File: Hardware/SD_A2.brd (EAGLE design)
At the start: 100.2 x 77.7 mm, 31 parts, among them IC1 74LS245N, IC2 LM317, IC4 XC9572XL, IC5 28C64ASO

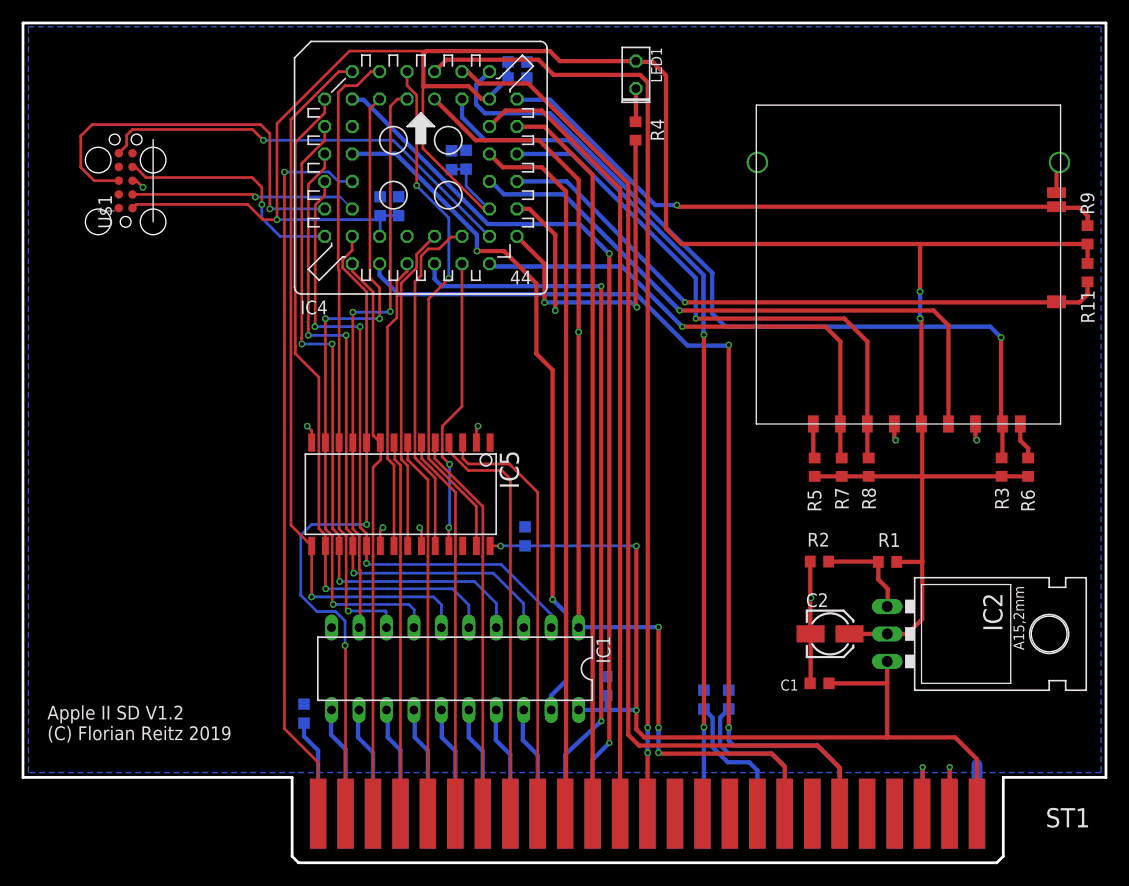
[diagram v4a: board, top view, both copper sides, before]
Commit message: Resistor network added
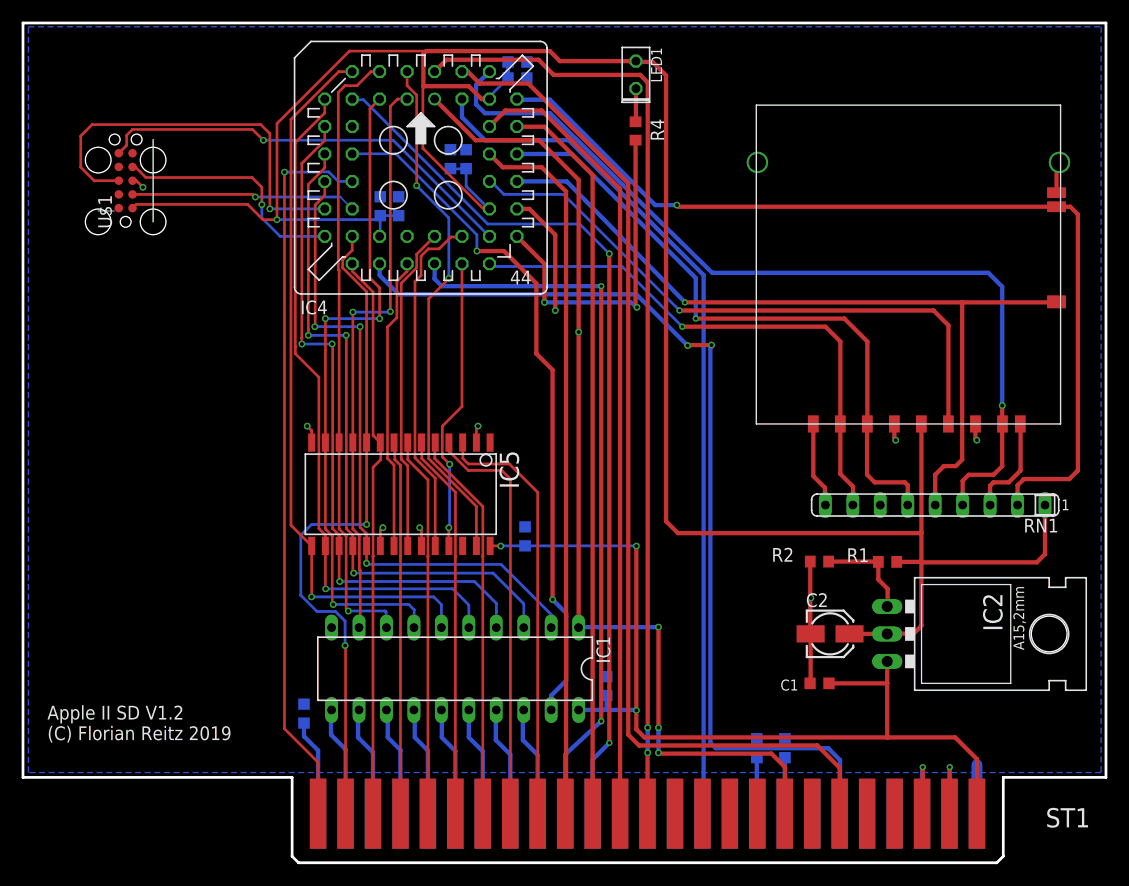
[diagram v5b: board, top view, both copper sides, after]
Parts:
- removed R11, R3, R5, R6, R7, R9: 100k, rcl:R0603
- removed R8: 68k, rcl:R0603
- added RN1: 100k, resistor-sil:SIL9
- moved C12 6.88 mm to (70.5, 10.5)
- moved C13 6.65 mm to (67.9, 10.5)
- moved C10 0.14 mm to (39.5, 65.0)
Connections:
- removed net N$2: R5.2, U$2.P9
- removed net N$3: R6.2, U$2.P8
- new net DAT1: RN1.3, U$2.P8
- new net DAT2: RN1.9, U$2.P9
- net !CS: now also RN1.8; no longer R7.1
- net +3V3: now also RN1.1; no longer R11.1, R3.2, R5.1, R6.1, R7.2, R8.2, R9.1
- net CARD: now also RN1.5; no longer R11.2
- net MISO: now also RN1.4; no longer R3.1
- net MOSI: now also RN1.6; no longer R8.1
- net WP: now also RN1.2; no longer R9.2
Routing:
- net WP: track 58.2 -> 88.0 mm
- net CARD: track 59.0 -> 75.1 mm
- net +3V3: track 230.4 -> 220.4 mm, vias 3 -> 1
- net -12V: track 14.8 -> 5.19 mm
- net DAT1: track 0.00 -> 9.50 mm
- net DAT2: track 0.00 -> 7.96 mm
- net MISO: track 74.4 -> 82.2 mm
- net -5V: track 12.9 -> 5.20 mm
- net MOSI: track 52.6 -> 60.1 mm
- net !CS: track 46.3 -> 51.1 mm
- net N$3: track 3.45 -> 0.00 mm
- net N$2: track 3.20 -> 0.00 mm
- net !RESET: track 88.2 -> 88.9 mm
- net 7M: vias 2 -> 0

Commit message: Trace width 0.254
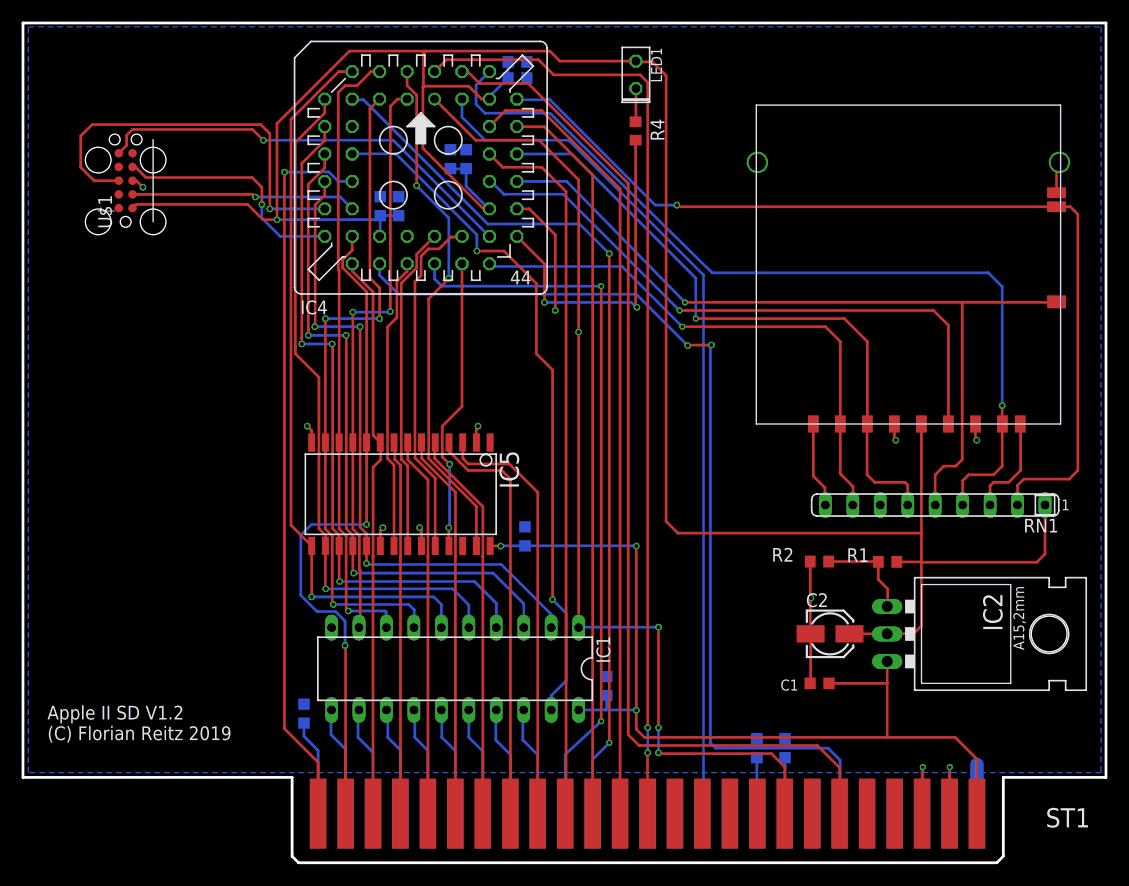
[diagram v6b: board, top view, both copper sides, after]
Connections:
- net N$5 renamed DMA
- net N$6 renamed INT

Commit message: Keepout for Tag Connect
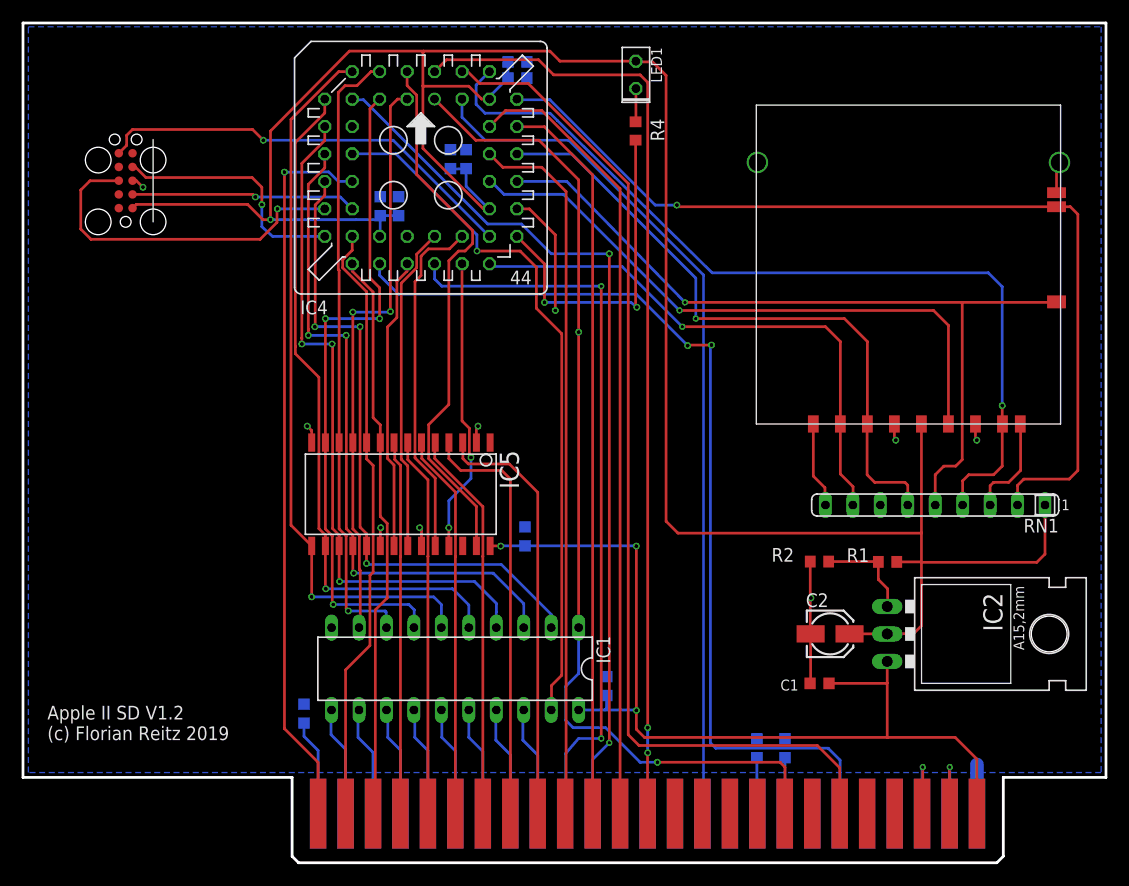
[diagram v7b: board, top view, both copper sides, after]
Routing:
- net ADD0: track 62.9 -> 56.0 mm, vias 2 -> 0
- net TDI: track 37.2 -> 32.3 mm
- net !WE: track 48.1 -> 50.3 mm, vias 2 -> 0
- net !DEV_SEL: track 67.4 -> 68.5 mm
- net !G: track 64.1 -> 64.6 mm, vias 2 -> 1
- net R/!W: track 93.6 -> 93.4 mm, vias 4 -> 2
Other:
- board text added: "Apple II SD V1.2 (c) Florian Reitz 2019"
- board text removed: "Apple II SD V1.2 (C) Florian Reitz 2019"

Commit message: Rename in AII connector
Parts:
- ST1: value (none) -> A2-50PINSLOT1-3
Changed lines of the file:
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@@
 </autorouter>
 <elements>
-<element name="ST1" library="con-apple2" package="A2-50PIN-SL1-3" value="" x="100.33" y="0" smashed="yes">
+<element name="ST1" library="con-apple2" package="A2-50PIN-SL1-3" value="A2-50PINSLOT1-3" x="100.33" y="0" smashed="yes">
 <attribute name="VALUE" x="94.615" y="-0.635" size="1.778" layer="27"/>
 </element>
